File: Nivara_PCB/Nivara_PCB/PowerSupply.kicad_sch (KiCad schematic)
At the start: 19 parts, among them U4 AP63200WU

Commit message: TERMINACIONES Y AJUSTES FINALES
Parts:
- removed C4: 10uF, PCM_Capacitor_SMD_AKL:C_1206_3216Metric, symbol EasyEDA:C_1206
- removed C7, C8: 22uF, PCM_Capacitor_SMD_AKL:C_0603_1608Metric, symbol EasyEDA:C_0603
- removed D38, D4: IR26-21C_L110_TR8, LED_SMD:LED_1206_3216Metric, symbol LED:IR26-21C_L110_TR8
- removed R3: 1k2, PCM_Resistor_SMD_AKL:R_0603_1608Metric, symbol EasyEDA:R_0603
- added C21, C22: 22uF, PCM_Capacitor_SMD_AKL:C_0805_2012Metric, symbol EasyEDA:C_0805
- added C4: 10uF, Capacitor_SMD:CP_Elec_4x5.4, symbol Device:C_Polarized
- added D5: LED_R, LED_SMD:LED_0603_1608Metric, symbol EasyEDA:LED
- added D6: LED, LED_SMD:LED_0603_1608Metric, symbol EasyEDA:LED
- added R8: 1.5k, PCM_Resistor_SMD_AKL:R_0603_1608Metric, symbol EasyEDA:R_0603
- C5: LCSC Part (none) -> C56476; Part # (none) -> C1608X7R1H104KT000N
- C6: LCSC Part (none) -> C76709; Part # (none) -> CGA3E2C0G1H101JT0Y0N
- L1: value CXP0420-6R8M-AG(6.8UH) -> HCMA-0420-6R8-M; LCSC Part C7461340 -> C351092; Part # (none) -> YSPI0420-6R8M
- R10: renamed from R5; LCSC Part (none) -> C136961; Part # (none) -> RT0603BRD0762KL
- R11: renamed from R6; LCSC Part (none) -> C22775; Part # (none) -> 0603WAF1000T5E
- R9: renamed from R4; LCSC Part (none) -> C2974032; Part # (none) -> FRC0603F1963TS
- TP1, TP2, TP3, TP4, TP5: now left out of the parts list
- U6: renamed from U4; LCSC Part (none) -> C2071868; Part # (none) -> AP63200WU-7
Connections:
- net +3.3V: now also D6.2 (A)
- net GND: now also C21.1, C22.1, C4.2, R8.2
- net VCC: now also C4.1, D5.2 (A)
- net VOUT: now also C21.2, C22.2
- net at R11.2: now also D6.1 (K)
- new net: D5.1 (K), R8.1

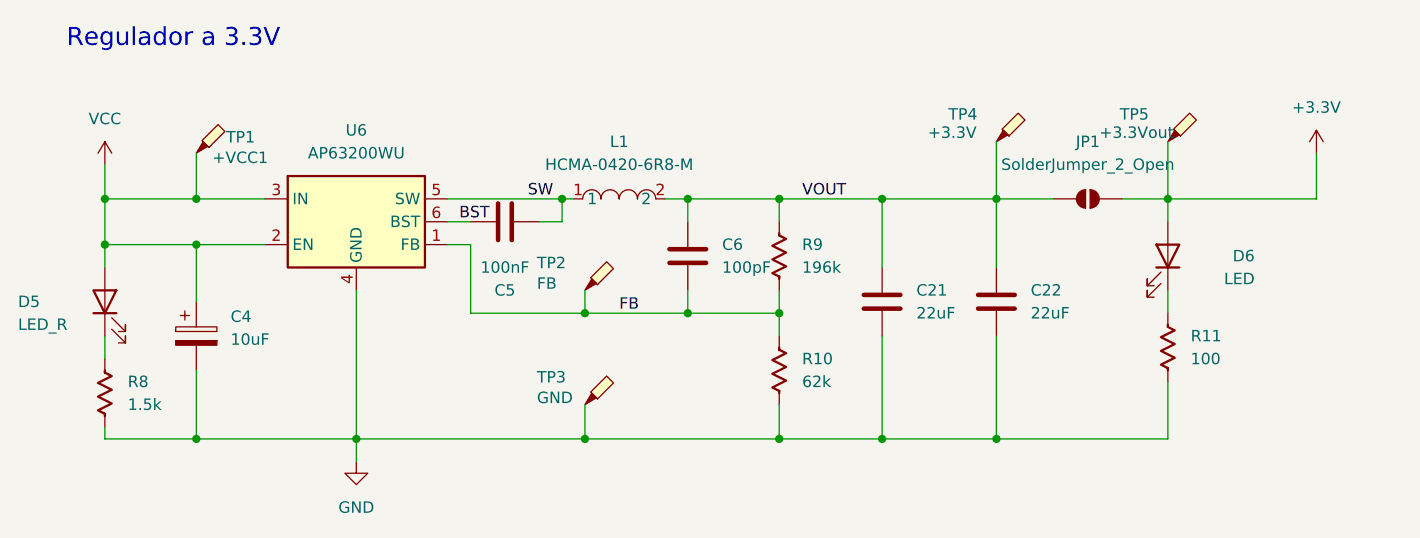
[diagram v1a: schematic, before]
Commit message: Cambios en las silscreen de los componentes.
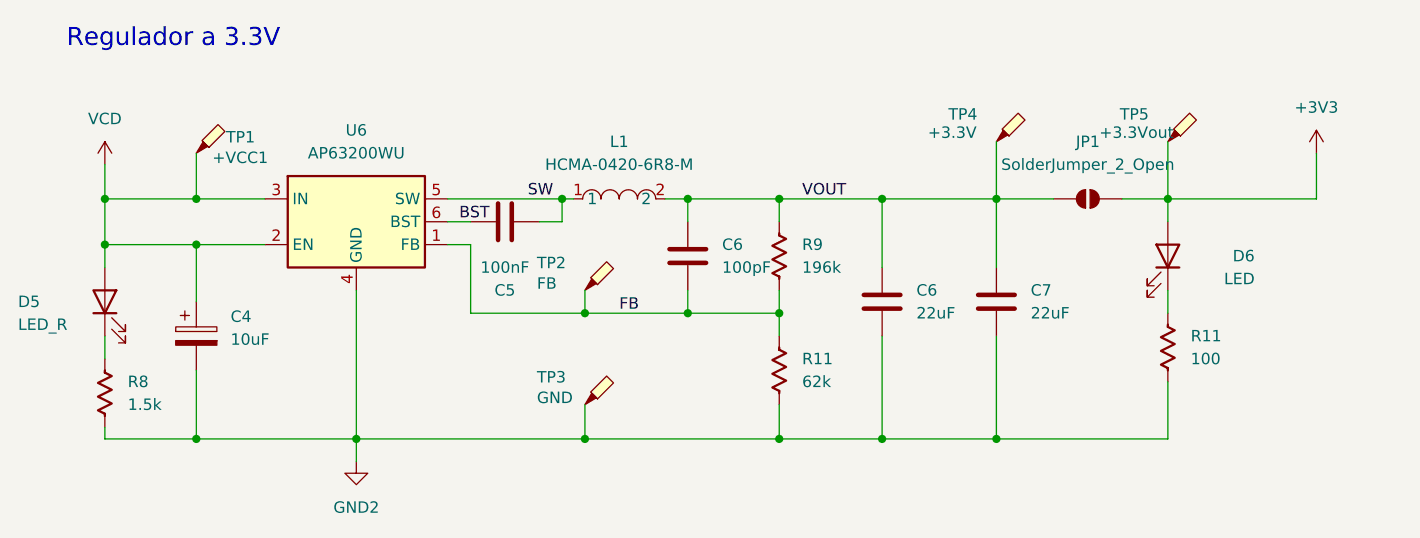
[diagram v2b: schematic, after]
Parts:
- renumbered C21 to C6, C22 to C7, R10 to R11
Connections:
- net +3.3V renamed +3V3
- net GND renamed GND2
- net VCC renamed VCD
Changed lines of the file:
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@@
 		(on_board yes)
 		(dnp no)
-		(property "Reference" "C21"
+		(property "Reference" "C6"
 			(at 133.35 57.1499 0)
 			(effects
@@
 			(project "Nivara_PCB"
 				(path "/13184db0-a71d-4054-b13a-bbf46d2b100d/4e7fa7f2-8bf5-4f9c-874d-fa1b4fd76f92/c8cd749e-9134-4d76-b8ef-ce0eb3eb606f"
-					(reference "C21")
+					(reference "C6")
 					(unit 1)
 				)
@@
 				(path "/13184db0-a71d-4054-b13a-bbf46d2b100d/4e7fa7f2-8bf5-4f9c-874d-fa1b4fd76f92/c8cd749e-9134-4d76-b8ef-ce0eb3eb606f"
 					(reference "C4")
+					(unit 1)
+				)
+			)
+		)
+	)
+	(symbol
+		(lib_id "EasyEDA:VCC")
+		(at 43.18 43.18 0)
+		(unit 1)
+		(exclude_from_sim no)
+		(in_bom yes)
+		(on_board yes)
+		(dnp no)
+		(fields_autoplaced yes)
+		(property "Reference" "#PWR025"
+			(at 43.18 46.99 0)
+			(effects
+				(font
+					(size 1.27 1.27)
+				)
+				(hide yes)
+			)
+		)
+		(property "Value" "VCD"
+			(at 43.18 38.1 0)
+			(effects
+				(font
+					(size 1.27 1.27)
+				)
+			)
+		)
+		(property "Footprint" ""
+			(at 43.18 43.18 0)
+			(effects
+				(font
+					(size 1.27 1.27)
+				)
+				(hide yes)
+			)
+		)
+		(property "Datasheet" ""
+			(at 43.18 43.18 0)
+			(effects
+				(font
+					(size 1.27 1.27)
+				)
+				(hide yes)
+			)
+		)
+		(property "Description" "Power symbol creates a global label with name \"VCC\""
+			(at 43.18 43.18 0)
+			(effects
+				(font
+					(size 1.27 1.27)
+				)
+				(hide yes)
+			)
+		)
+		(pin "1"
+		)
+		(instances
+			(project "Nivara_PCB"
+				(path "/13184db0-a71d-4054-b13a-bbf46d2b100d/4e7fa7f2-8bf5-4f9c-874d-fa1b4fd76f92/c8cd749e-9134-4d76-b8ef-ce0eb3eb606f"
+					(reference "#PWR025")
 					(unit 1)
 				)
@@
 		)
 		(instances
-			(project ""
+			(project "Nivara_PCB"
 				(path "/13184db0-a71d-4054-b13a-bbf46d2b100d/4e7fa7f2-8bf5-4f9c-874d-fa1b4fd76f92/c8cd749e-9134-4d76-b8ef-ce0eb3eb606f"
 					(reference "U6")
+					(unit 1)
+				)
+			)
+		)
+	)
+	(symbol
+		(lib_id "EasyEDA:+3.3V")
+		(at 177.8 41.91 0)
+		(unit 1)
+		(exclude_from_sim no)
+		(in_bom yes)
+		(on_board yes)
+		(dnp no)
+		(property "Reference" "#PWR027"
+			(at 177.8 45.72 0)
+			(effects
+				(font
+					(size 1.27 1.27)
+				)
+				(hide yes)
+			)
+		)
+		(property "Value" "+3V3"
+			(at 177.8 36.83 0)
+			(effects
+				(font
+					(size 1.27 1.27)
+				)
+			)
+		)
+		(property "Footprint" ""
+			(at 177.8 41.91 0)
+			(effects
+				(font
+					(size 1.27 1.27)
+				)
+				(hide yes)
+			)
+		)
+		(property "Datasheet" ""
+			(at 177.8 41.91 0)
+			(effects
+				(font
+					(size 1.27 1.27)
+				)
+				(hide yes)
+			)
+		)
+		(property "Description" "Power symbol creates a global label with name \"+3.3V\""
+			(at 177.8 41.91 0)
+			(effects
+				(font
+					(size 1.27 1.27)
+				)
+				(hide yes)
+			)
+		)
+		(pin "1"
+		)
+		(instances
+			(project "Nivara_PCB"
+				(path "/13184db0-a71d-4054-b13a-bbf46d2b100d/4e7fa7f2-8bf5-4f9c-874d-fa1b4fd76f92/c8cd749e-9134-4d76-b8ef-ce0eb3eb606f"
+					(reference "#PWR027")
 					(unit 1)
 				)
@@
 		)
 		(instances
-			(project ""
+			(project "Nivara_PCB"
 				(path "/13184db0-a71d-4054-b13a-bbf46d2b100d/4e7fa7f2-8bf5-4f9c-874d-fa1b4fd76f92/c8cd749e-9134-4d76-b8ef-ce0eb3eb606f"
 					(reference "R9")
@@
 		(on_board yes)
 		(dnp no)
-		(property "Reference" "C22"
+		(property "Reference" "C7"
 			(at 146.05 57.1499 0)
 			(effects
@@
 			(project "Nivara_PCB"
 				(path "/13184db0-a71d-4054-b13a-bbf46d2b100d/4e7fa7f2-8bf5-4f9c-874d-fa1b4fd76f92/c8cd749e-9134-4d76-b8ef-ce0eb3eb606f"
-					(reference "C22")
-					(unit 1)
-				)
-			)
-		)
-	)
-	(symbol
-		(lib_id "EasyEDA:GND")
-		(at 71.12 76.2 0)
-		(unit 1)
-		(exclude_from_sim no)
-		(in_bom yes)
-		(on_board yes)
-		(dnp no)
-		(fields_autoplaced yes)
-		(property "Reference" "#PWR024"
-			(at 71.12 82.55 0)
-			(effects
-				(font
-					(size 1.27 1.27)
-				)
-				(hide yes)
-			)
-		)
-		(property "Value" "GND"
-			(at 71.12 81.28 0)
-			(effects
-				(font
-					(size 1.27 1.27)
-				)
-			)
-		)
-		(property "Footprint" ""
-			(at 71.12 76.2 0)
-			(effects
-				(font
-					(size 1.27 1.27)
-				)
-				(hide yes)
-			)
-		)
-		(property "Datasheet" ""
-			(at 71.12 76.2 0)
-			(effects
-				(font
-					(size 1.27 1.27)
-				)
-				(hide yes)
-			)
-		)
-		(property "Description" "Power symbol creates a global label with name \"GND\" , ground"
-			(at 71.12 76.2 0)
-			(effects
-				(font
-					(size 1.27 1.27)
-				)
-				(hide yes)
-			)
-		)
-		(pin "1"
-		)
-		(instances
-			(project ""
-				(path "/13184db0-a71d-4054-b13a-bbf46d2b100d/4e7fa7f2-8bf5-4f9c-874d-fa1b4fd76f92/c8cd749e-9134-4d76-b8ef-ce0eb3eb606f"
-					(reference "#PWR024")
+					(reference "C7")
 					(unit 1)
 				)
@@
 		(dnp no)
 		(fields_autoplaced yes)
-		(property "Reference" "R10"
+		(property "Reference" "R11"
 			(at 120.65 64.7699 0)
 			(effects
@@
 			(project "Nivara_PCB"
 				(path "/13184db0-a71d-4054-b13a-bbf46d2b100d/4e7fa7f2-8bf5-4f9c-874d-fa1b4fd76f92/c8cd749e-9134-4d76-b8ef-ce0eb3eb606f"
-					(reference "R10")
+					(reference "R11")
 					(unit 1)
 				)
@@
 	)
 	(symbol
-		(lib_id "EasyEDA:+3.3V")
-		(at 177.8 41.91 0)
+		(lib_id "power:GND2")
+		(at 71.12 76.2 0)
 		(unit 1)
 		(exclude_from_sim no)
@@
 		(dnp no)
 		(fields_autoplaced yes)
-		(property "Reference" "#PWR025"
-			(at 177.8 45.72 0)
-			(effects
-				(font
-					(size 1.27 1.27)
-				)
-				(hide yes)
-			)
-		)
-		(property "Value" "+3.3V"
-			(at 177.8 36.83 0)
+		(property "Reference" "#PWR026"
+			(at 71.12 82.55 0)
+			(effects
+				(font
+					(size 1.27 1.27)
+				)
+				(hide yes)
+			)
+		)
+		(property "Value" "GND2"
+			(at 71.12 81.28 0)
 			(effects
 				(font
@@
 		)
 		(property "Footprint" ""
-			(at 177.8 41.91 0)
+			(at 71.12 76.2 0)
 			(effects
 				(font
@@
 		)
 		(property "Datasheet" ""
-			(at 177.8 41.91 0)
-			(effects
-				(font
-					(size 1.27 1.27)
-				)
-				(hide yes)
-			)
-		)
-		(property "Description" "Power symbol creates a global label with name \"+3.3V\""
-			(at 177.8 41.91 0)
-			(effects
-				(font
-					(size 1.27 1.27)
-				)
-				(hide yes)
-			)
-		)
-		(pin "1"
-		)
-		(instances
-			(project "Nivara_PCB"
-				(path "/13184db0-a71d-4054-b13a-bbf46d2b100d/4e7fa7f2-8bf5-4f9c-874d-fa1b4fd76f92/c8cd749e-9134-4d76-b8ef-ce0eb3eb606f"
-					(reference "#PWR025")
-					(unit 1)
-				)
-			)
-		)
-	)
-	(symbol
-		(lib_id "EasyEDA:VCC")
-		(at 43.18 43.18 0)
-		(unit 1)
-		(exclude_from_sim no)
-		(in_bom yes)
-		(on_board yes)
-		(dnp no)
-		(fields_autoplaced yes)
-		(property "Reference" "#PWR023"
-			(at 43.18 46.99 0)
-			(effects
-				(font
-					(size 1.27 1.27)
-				)
-				(hide yes)
-			)
-		)
-		(property "Value" "VCC"
-			(at 43.18 38.1 0)
-			(effects
-				(font
-					(size 1.27 1.27)
-				)
-			)
-		)
-		(property "Footprint" ""
-			(at 43.18 43.18 0)
-			(effects
-				(font
-					(size 1.27 1.27)
-				)
-				(hide yes)
-			)
-		)
-		(property "Datasheet" ""
-			(at 43.18 43.18 0)
-			(effects
-				(font
-					(size 1.27 1.27)
-				)
-				(hide yes)
-			)
-		)
-		(property "Description" "Power symbol creates a global label with name \"VCC\""
-			(at 43.18 43.18 0)
-			(effects
-				(font
-					(size 1.27 1.27)
-				)
-				(hide yes)
-			)
-		)
-		(pin "1"
-		)
-		(instances
-			(project "Nivara_PCB"
-				(path "/13184db0-a71d-4054-b13a-bbf46d2b100d/4e7fa7f2-8bf5-4f9c-874d-fa1b4fd76f92/c8cd749e-9134-4d76-b8ef-ce0eb3eb606f"
-					(reference "#PWR023")
+			(at 71.12 76.2 0)
+			(effects
+				(font
+					(size 1.27 1.27)
+				)
+				(hide yes)
+			)
+		)
+		(property "Description" "Power symbol creates a global label with name \"GND2\" , ground"
+			(at 71.12 76.2 0)
+			(effects
+				(font
+					(size 1.27 1.27)
+				)
+				(hide yes)
+			)
+		)
+		(pin "1"
+		)
+		(instances
+			(project "Nivara_PCB"
+				(path "/13184db0-a71d-4054-b13a-bbf46d2b100d/4e7fa7f2-8bf5-4f9c-874d-fa1b4fd76f92/c8cd749e-9134-4d76-b8ef-ce0eb3eb606f"
+					(reference "#PWR026")
 					(unit 1)
 				)
@@
 		)
 		(instances
-			(project ""
+			(project "Nivara_PCB"
 				(path "/13184db0-a71d-4054-b13a-bbf46d2b100d/4e7fa7f2-8bf5-4f9c-874d-fa1b4fd76f92/c8cd749e-9134-4d76-b8ef-ce0eb3eb606f"
 					(reference "JP1")
@@
 		)
 		(instances
-			(project ""
+			(project "Nivara_PCB"
 				(path "/13184db0-a71d-4054-b13a-bbf46d2b100d/4e7fa7f2-8bf5-4f9c-874d-fa1b4fd76f92/c8cd749e-9134-4d76-b8ef-ce0eb3eb606f"
 					(reference "L1")
@@
 		)
 		(instances
-			(project ""
+			(project "Nivara_PCB"
 				(path "/13184db0-a71d-4054-b13a-bbf46d2b100d/4e7fa7f2-8bf5-4f9c-874d-fa1b4fd76f92/c8cd749e-9134-4d76-b8ef-ce0eb3eb606f"
 					(reference "TP1")

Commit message: Ya está la pcb hecha y el pedido de los componentes realizado, falta soldar y probar.
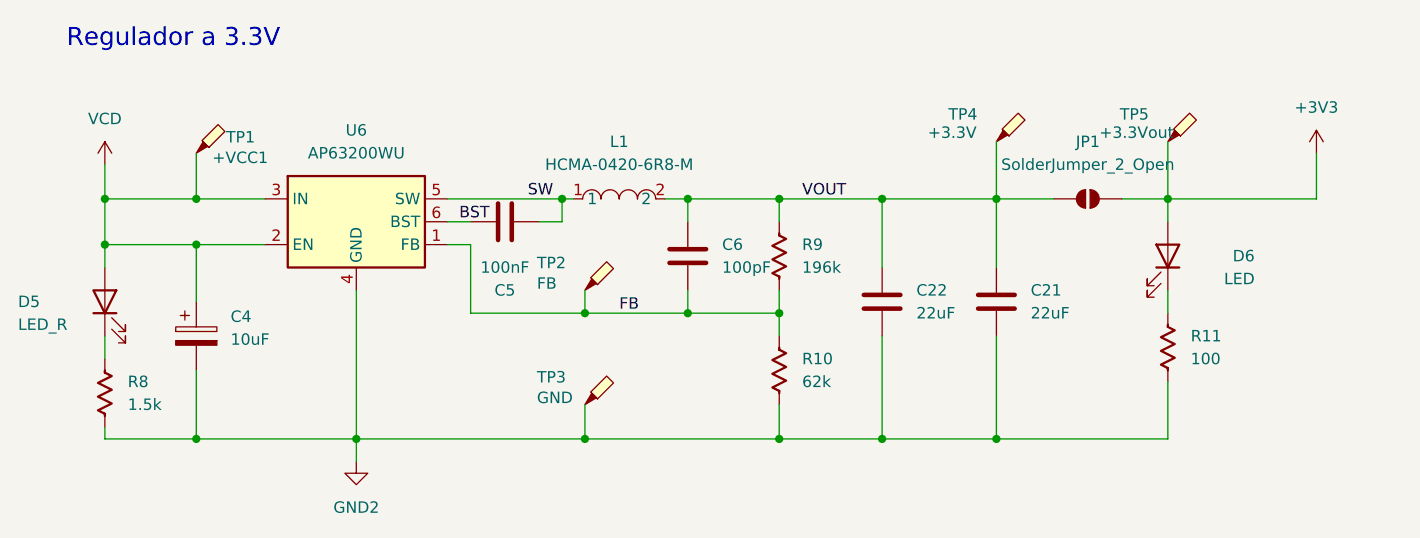
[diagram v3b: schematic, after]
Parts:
- D5: LCSC Part C2286 -> C84263; Part # KT-0603R -> NCD0603R1
- renumbered C7 to C21, C6 to C22, R11 to R10
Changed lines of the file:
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@@
 		(on_board yes)
 		(dnp no)
-		(property "Reference" "C6"
+		(property "Reference" "C22"
 			(at 133.35 57.1499 0)
 			(effects
@@
 			(project "Nivara_PCB"
 				(path "/13184db0-a71d-4054-b13a-bbf46d2b100d/4e7fa7f2-8bf5-4f9c-874d-fa1b4fd76f92/c8cd749e-9134-4d76-b8ef-ce0eb3eb606f"
-					(reference "C6")
+					(reference "C22")
 					(unit 1)
 				)
@@
 			)
 		)
-		(property "Datasheet" "https://jlcpcb.com/api/file/downloadByFileSystemAccessId/8550723991833485312"
+		(property "Datasheet" "https://www.lcsc.com/datasheet/C84263.pdf"
 			(at 43.18 58.42 0)
 			(effects
@@
 			)
 		)
-		(property "LCSC Part" "C2286"
+		(property "LCSC Part" "C84263"
 			(at 43.18 58.42 90)
 			(effects
@@
 			)
 		)
-		(property "Part #" "KT-0603R"
+		(property "Part #" "NCD0603R1"
 			(at 43.18 58.42 90)
 			(effects
@@
 		(on_board yes)
 		(dnp no)
-		(property "Reference" "C7"
+		(property "Reference" "C21"
 			(at 146.05 57.1499 0)
 			(effects
@@
 			(project "Nivara_PCB"
 				(path "/13184db0-a71d-4054-b13a-bbf46d2b100d/4e7fa7f2-8bf5-4f9c-874d-fa1b4fd76f92/c8cd749e-9134-4d76-b8ef-ce0eb3eb606f"
-					(reference "C7")
+					(reference "C21")
 					(unit 1)
 				)
@@
 		(dnp no)
 		(fields_autoplaced yes)
-		(property "Reference" "R11"
+		(property "Reference" "R10"
 			(at 120.65 64.7699 0)
 			(effects
@@
 			(project "Nivara_PCB"
 				(path "/13184db0-a71d-4054-b13a-bbf46d2b100d/4e7fa7f2-8bf5-4f9c-874d-fa1b4fd76f92/c8cd749e-9134-4d76-b8ef-ce0eb3eb606f"
-					(reference "R11")
-					(unit 1)
-				)
+					(reference "R10")
+					(unit 1)
+				)
